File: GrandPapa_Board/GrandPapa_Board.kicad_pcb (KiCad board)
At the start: 4 copper layers, 82 x 82 mm, 98 parts, among them J1 3.7V LiPo Single Cell, J11 Dupont 01x04_Male, J2 HARWIN_ROCKET, J3 Dupont_GPS, J4 HARWIN_MINISENSOR, J5 Dupont_Logger, J6 PROG Header, J7 HARWIN_KALMAN, J8 Therm EN Jumper, U1 MCP1642B-50I/MS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

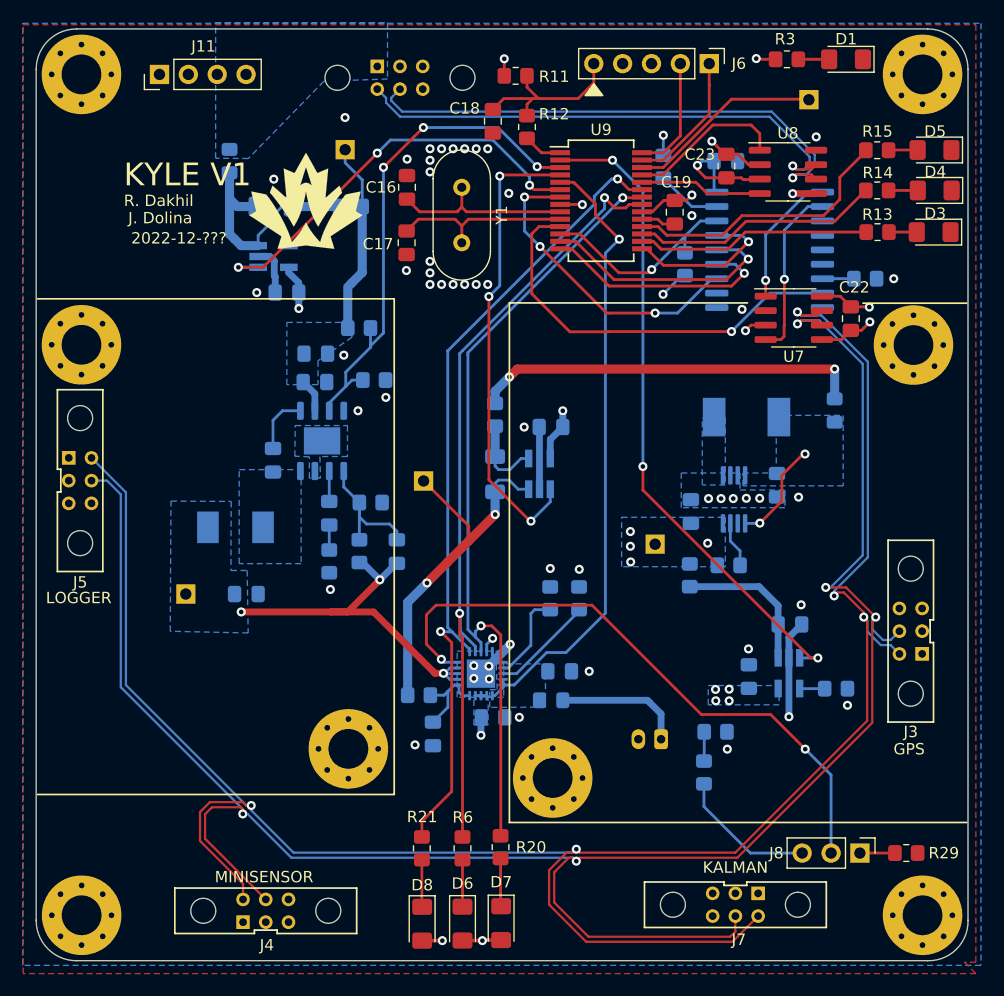
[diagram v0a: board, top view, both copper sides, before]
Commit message: minor PCB changes, fix logger mounting hole placement, minor schematic cleanup
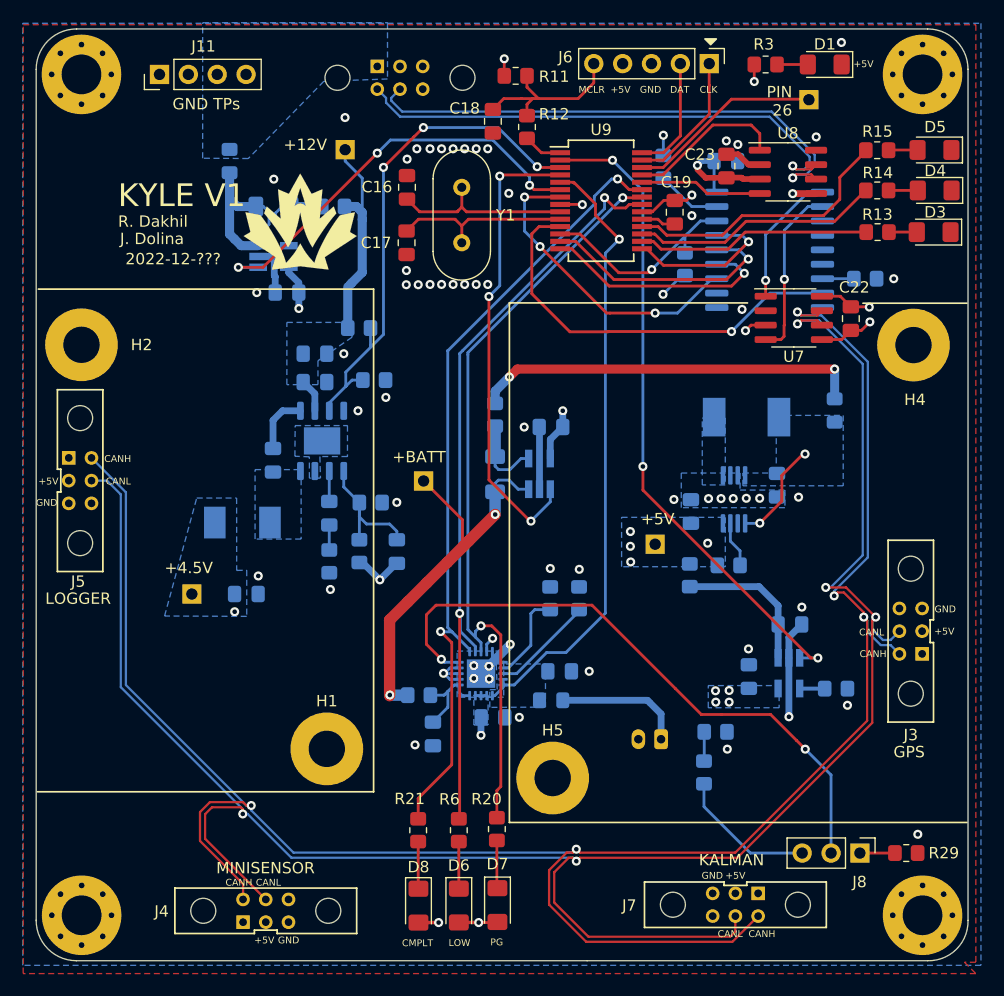
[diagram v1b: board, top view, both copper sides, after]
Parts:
- H1, H2, H4, H5: footprint MountingHole:MountingHole_3.5mm_Pad_Via -> MountingHole:MountingHole_3.2mm_M3_Pad
- moved D1 1.93 mm to (182.7, 63.4)
- moved R3 1.93 mm to (177.5, 63.4)
- moved G*** 1.90 mm to (136.5, 77.2)
- moved H1 1.90 mm to (138.9, 123.6)
- moved R21 1.62 mm to (146.9, 130.8)
- moved D6 1.62 mm to (150.5, 137.4)
- moved D7 1.62 mm to (153.9, 137.3)
- moved R20 1.62 mm to (153.8, 130.7)
- moved R6 1.62 mm to (150.5, 130.8)
- moved D8 1.62 mm to (146.9, 137.4)
- moved R9 1.56 mm to (139.4, 75.9)
- moved L1 0.73 mm to (131.4, 103.7)
- moved TP1 0.54 mm to (127.0, 110.0)
- moved C1 0.07 mm to (137.8, 88.8)
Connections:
- H1 pad 1: GND -> unconnected-(H1-Pad1)
- H2 pad 1: GND -> unconnected-(H2-Pad1)
- H4 pad 1: GND -> unconnected-(H4-Pad1)
- H5 pad 1: GND -> unconnected-(H5-Pad1)
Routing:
- net +4.5V: track 43.5 -> 18.0 mm
- net Net-(R22-Pad2): track 32.2 -> 34.7 mm
- net Net-(C1-Pad1): track 19.8 -> 21.6 mm
- net GND: track 41.3 -> 39.6 mm, vias 55 -> 60
- net /Battery Charging/BATT_CHARGE_COMPLETE: track 69.4 -> 67.7 mm
- net Net-(R1-Pad1): track 9.22 -> 7.66 mm
- net /Battery Charging/LOW_BAT: track 68.7 -> 67.3 mm
- net /Battery Charging/BATT_CHARGER_PG: track 72.0 -> 70.6 mm
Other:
- board text added: "CANH"
- board text added: "CANL"
- board text added: "CLK"
- board text added: "CMPLT"
- board text added: "DAT"
- board text added: "GND"
- board text added: "GND TPs"
- board text added: "LOW"
- board text added: "MCLR"
- board text added: "PG"
